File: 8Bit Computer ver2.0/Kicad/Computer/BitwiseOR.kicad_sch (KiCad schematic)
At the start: 5 parts, among them IC34 SN74LVC1G14DBVR, IC39 SN74ABT574ADWR, IC44 SN74AHC32DR, IC45 SN74AHC32DR, IC59 SN74AHC74DR

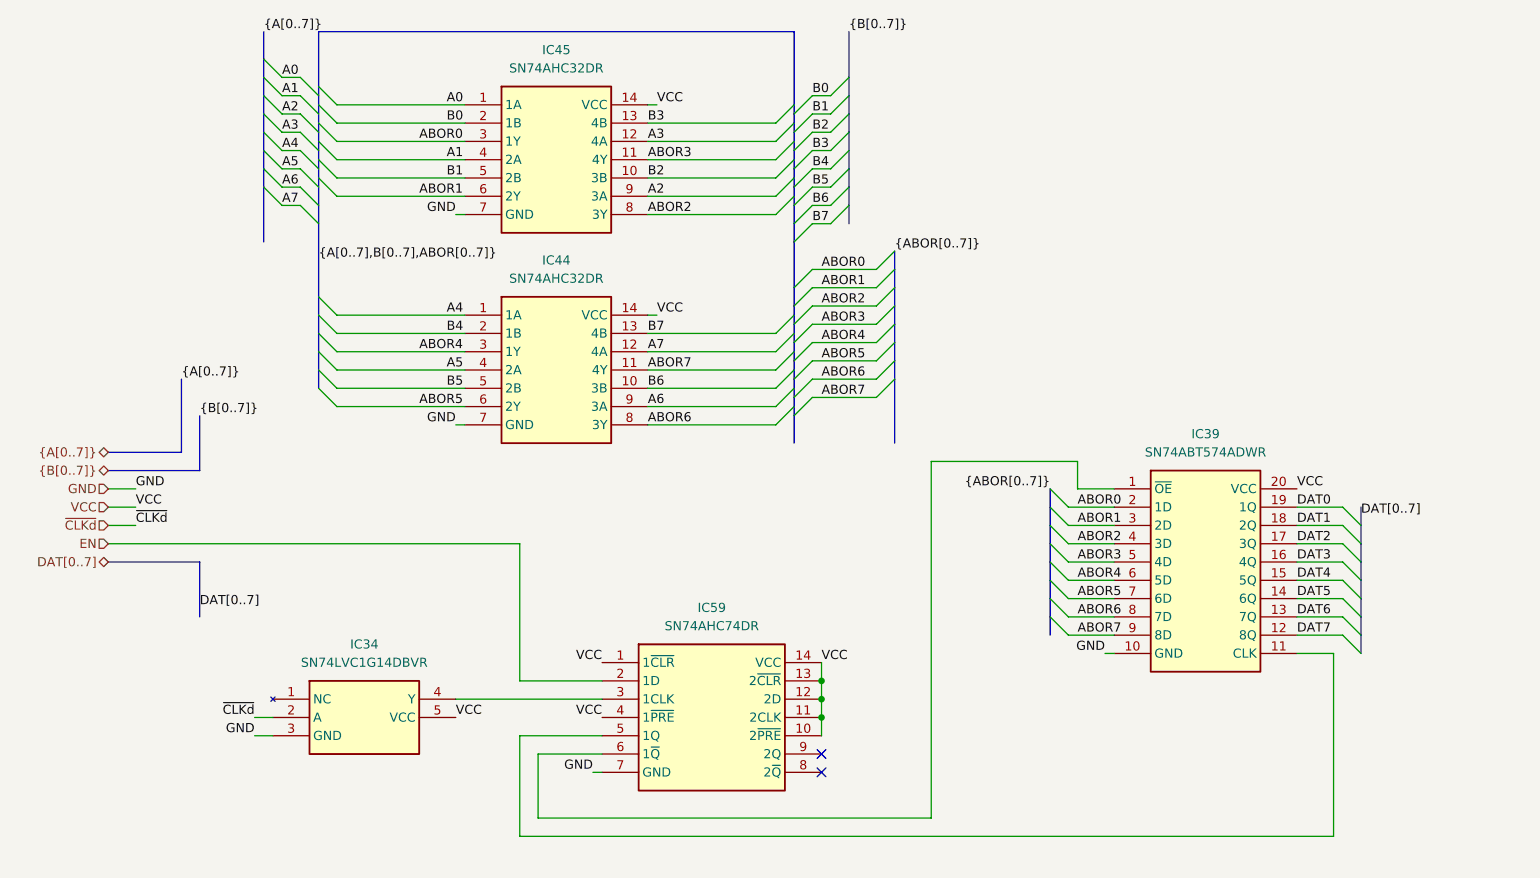
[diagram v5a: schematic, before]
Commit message: Kicad SCH/PCB
Kicad SCH/PCB:
changed the References in SCH
began with INOUTPUT module nearly done
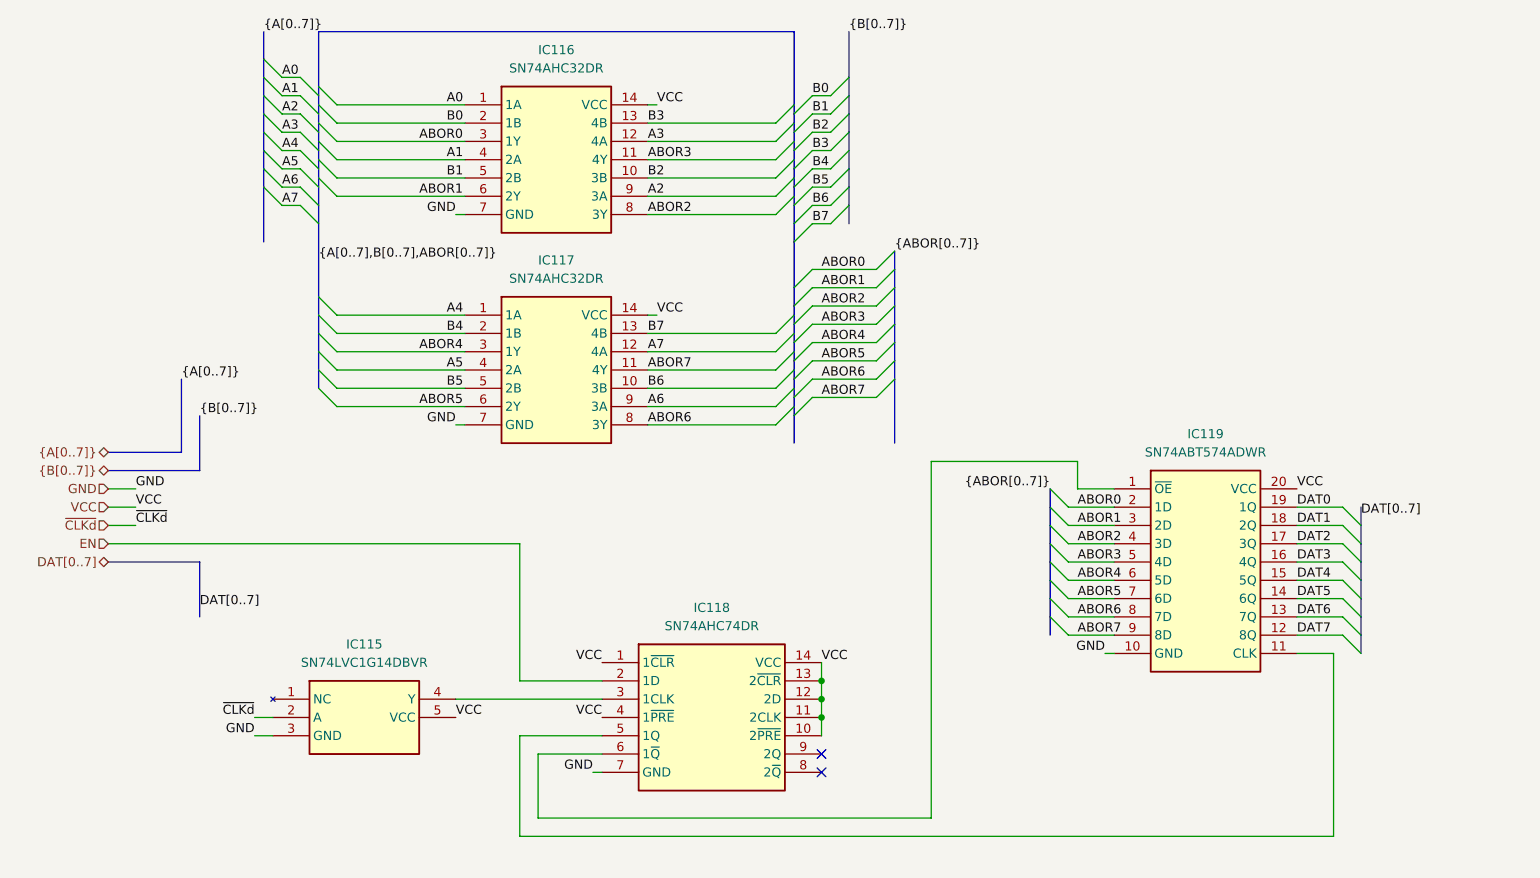
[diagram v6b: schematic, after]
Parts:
- renumbered IC34 to IC115, IC45 to IC116, IC44 to IC117, IC59 to IC118, IC39 to IC119
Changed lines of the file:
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@@
 		(dnp no)
 		(fields_autoplaced yes)
-		(property "Reference" "IC34"
+		(property "Reference" "IC115"
 			(at 80.01 118.11 0)
 			(effects
@@
 			(project "Computer"
 				(path "/1196a00e-6878-4d6d-82b7-9e052dfe7c14/c4d8b530-1c6d-45af-88d2-7dc1d4321a34/aa0223c1-ee7f-4786-bdbb-d5c154528f66"
-					(reference "IC34")
+					(reference "IC115")
 					(unit 1)
 				)
@@
 		(dnp no)
 		(fields_autoplaced yes)
-		(property "Reference" "IC44"
+		(property "Reference" "IC117"
 			(at 106.68 64.77 0)
 			(effects
@@
 			(project "Computer"
 				(path "/1196a00e-6878-4d6d-82b7-9e052dfe7c14/c4d8b530-1c6d-45af-88d2-7dc1d4321a34/aa0223c1-ee7f-4786-bdbb-d5c154528f66"
-					(reference "IC44")
+					(reference "IC117")
 					(unit 1)
 				)
@@
 		(dnp no)
 		(fields_autoplaced yes)
-		(property "Reference" "IC39"
+		(property "Reference" "IC119"
 			(at 196.85 88.9 0)
 			(effects
@@
 			(project "Computer"
 				(path "/1196a00e-6878-4d6d-82b7-9e052dfe7c14/c4d8b530-1c6d-45af-88d2-7dc1d4321a34/aa0223c1-ee7f-4786-bdbb-d5c154528f66"
-					(reference "IC39")
+					(reference "IC119")
 					(unit 1)
 				)
@@
 		(dnp no)
 		(fields_autoplaced yes)
-		(property "Reference" "IC59"
+		(property "Reference" "IC118"
 			(at 128.27 113.03 0)
 			(effects
@@
 			(project "Computer"
 				(path "/1196a00e-6878-4d6d-82b7-9e052dfe7c14/c4d8b530-1c6d-45af-88d2-7dc1d4321a34/aa0223c1-ee7f-4786-bdbb-d5c154528f66"
-					(reference "IC59")
+					(reference "IC118")
 					(unit 1)
 				)
@@
 		(dnp no)
 		(fields_autoplaced yes)
-		(property "Reference" "IC45"
+		(property "Reference" "IC116"
 			(at 106.68 35.56 0)
 			(effects
@@
 			(project "Computer"
 				(path "/1196a00e-6878-4d6d-82b7-9e052dfe7c14/c4d8b530-1c6d-45af-88d2-7dc1d4321a34/aa0223c1-ee7f-4786-bdbb-d5c154528f66"
-					(reference "IC45")
+					(reference "IC116")
 					(unit 1)
 				)

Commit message: changed page numbers, compressed ROOT file from A1 to A4
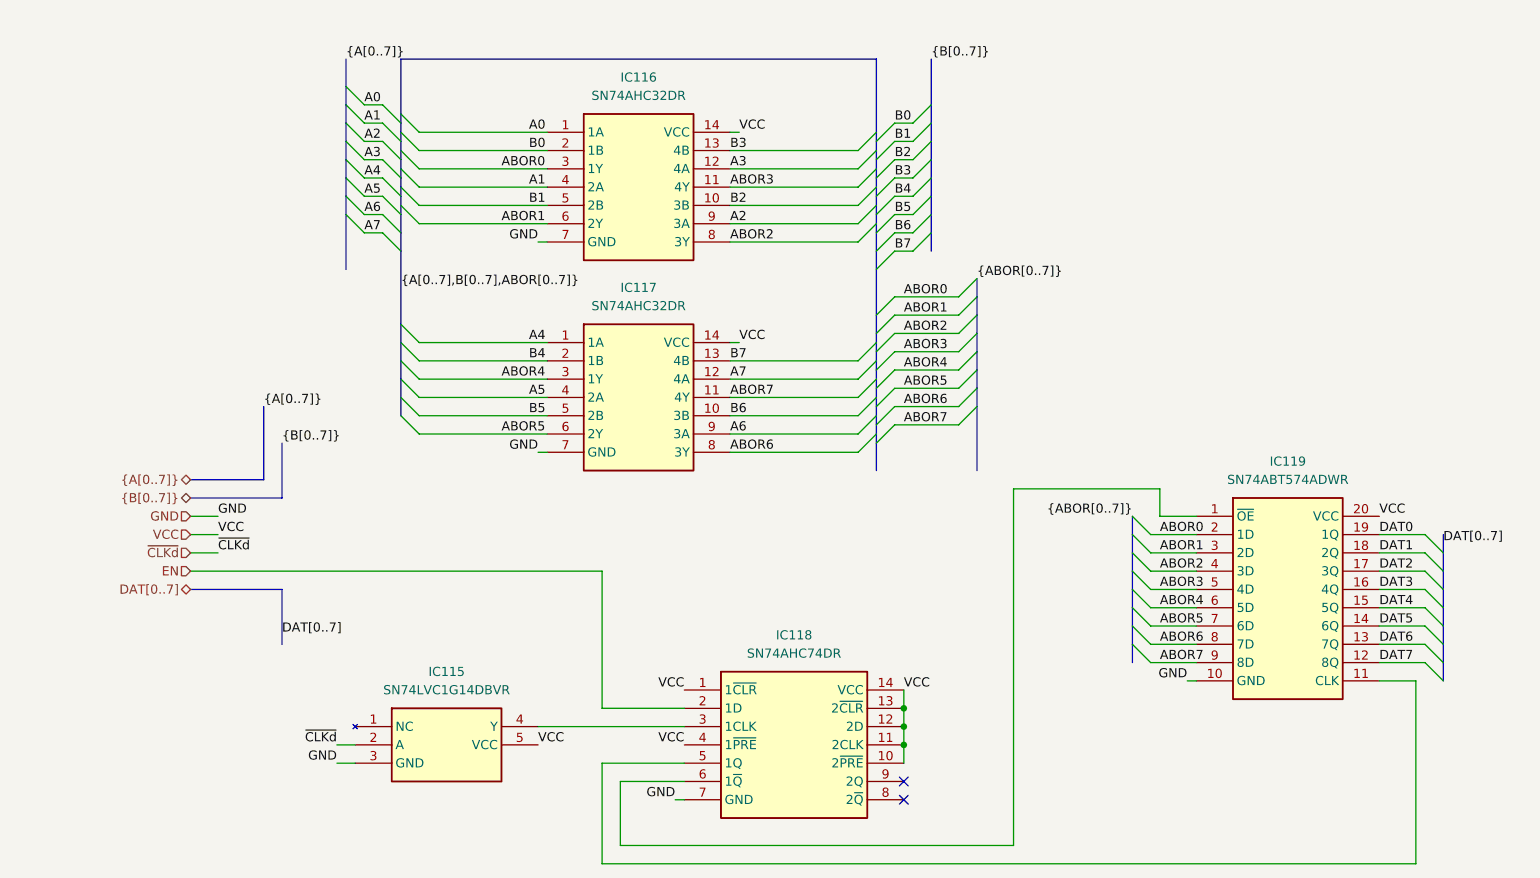
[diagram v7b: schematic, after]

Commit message: changed page numbers, every schematic is now A4
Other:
- title: (none) -> ${SHEETNAME}
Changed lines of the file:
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@@
 	(generator_version "9.0")
 	(paper "A4")
+	(title_block
+		(title "${SHEETNAME}")
+		(date "2026-03-21")
+		(rev "2.7")
+	)
 	(junction
 		(at 154.94 127)
